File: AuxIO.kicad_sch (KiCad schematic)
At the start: 1 part, among them J10 Conn_02x15_Odd_Even

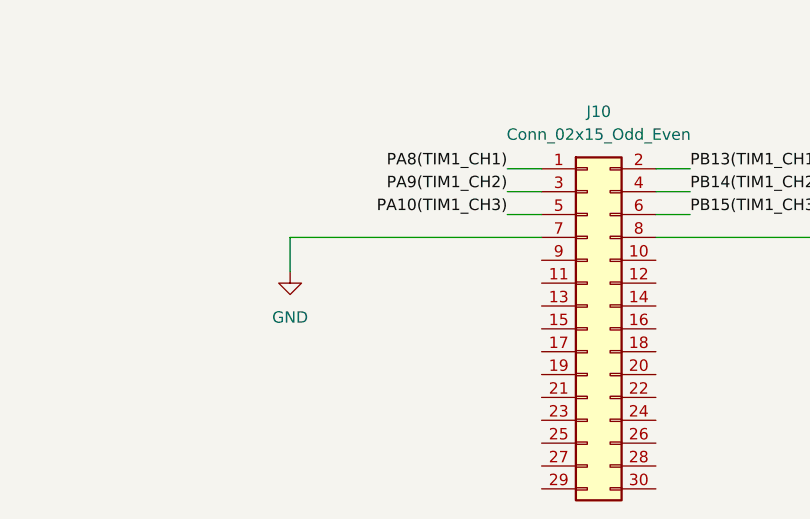
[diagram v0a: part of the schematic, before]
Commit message: Key CHanges for connector choices , termination and semi-final decisions on them
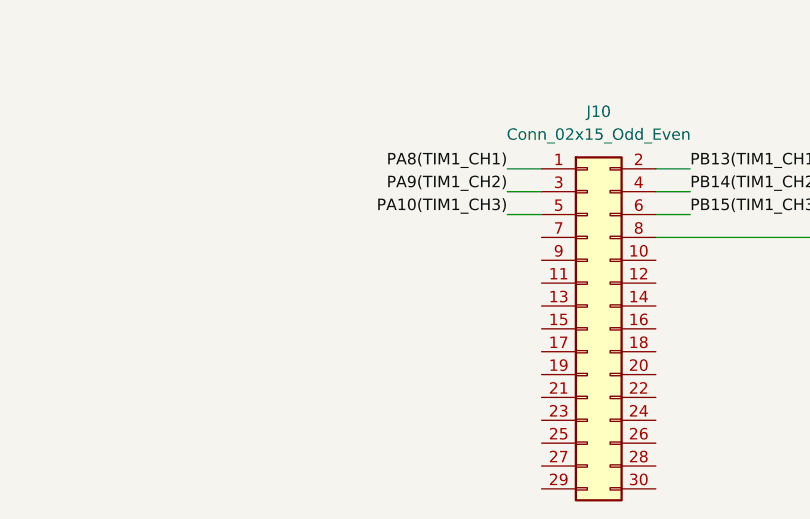
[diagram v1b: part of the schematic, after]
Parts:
- J10: footprint (none) -> Connector_IDC:IDC-Header_2x15_P2.54mm_Vertical
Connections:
- net GND: no longer J10.7 (Pin_7)
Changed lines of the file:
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@@
-	(wire
-		(pts
-			(xy 124.46 83.82) (xy 96.52 83.82)
-		)
-		(stroke
-			(width 0)
-			(type default)
-		)
-	)
 	(wire
 		(pts
@@
 		(pts
 			(xy 137.16 81.28) (xy 140.97 81.28)
-		)
-		(stroke
-			(width 0)
-			(type default)
-		)
-	)
-	(wire
-		(pts
-			(xy 96.52 83.82) (xy 96.52 87.63)
 		)
 		(stroke
@@
 			)
 			(justify left bottom)
-		)
-	)
-	(symbol
-		(lib_id "power:GND")
-		(at 96.52 87.63 0)
-		(unit 1)
-		(exclude_from_sim no)
-		(in_bom yes)
-		(on_board yes)
-		(dnp no)
-		(fields_autoplaced yes)
-		(property "Reference" "#PWR035"
-			(at 96.52 93.98 0)
-			(effects
-				(font
-					(size 1.27 1.27)
-				)
-				(hide yes)
-			)
-		)
-		(property "Value" "GND"
-			(at 96.52 92.71 0)
-			(effects
-				(font
-					(size 1.27 1.27)
-				)
-			)
-		)
-		(property "Footprint" ""
-			(at 96.52 87.63 0)
-			(effects
-				(font
-					(size 1.27 1.27)
-				)
-				(hide yes)
-			)
-		)
-		(property "Datasheet" ""
-			(at 96.52 87.63 0)
-			(effects
-				(font
-					(size 1.27 1.27)
-				)
-				(hide yes)
-			)
-		)
-		(property "Description" "Power symbol creates a global label with name \"GND\" , ground"
-			(at 96.52 87.63 0)
-			(effects
-				(font
-					(size 1.27 1.27)
-				)
-				(hide yes)
-			)
-		)
-		(pin "1"
-		)
-		(instances
-			(project "OhWare"
-				(path "/38f33acd-ac87-4918-9c1f-d78977d10c9f/49be7343-6876-4872-8ca7-768fcc55fbeb"
-					(reference "#PWR035")
-					(unit 1)
-				)
-			)
 		)
 	)
@@
 			)
 		)
-		(property "Footprint" ""
+		(property "Footprint" "Connector_IDC:IDC-Header_2x15_P2.54mm_Vertical"
 			(at 129.54 93.98 0)
 			(effects
